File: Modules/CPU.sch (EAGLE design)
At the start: 89 parts, among them IC4 93LC66SM, IC5 MIC2026-1YM, J1 USB_A_SMT_FEMALE, J2 USB_A_SMT_FEMALE, J4 SD_CARD_SOCKET, Q1 DMG1012T-7, Q2 DMG1012T-7, Q3 DMG1012T-7, U5 LAN9512-JZX, U6 FSUSB42UMX, Y2 25MHz

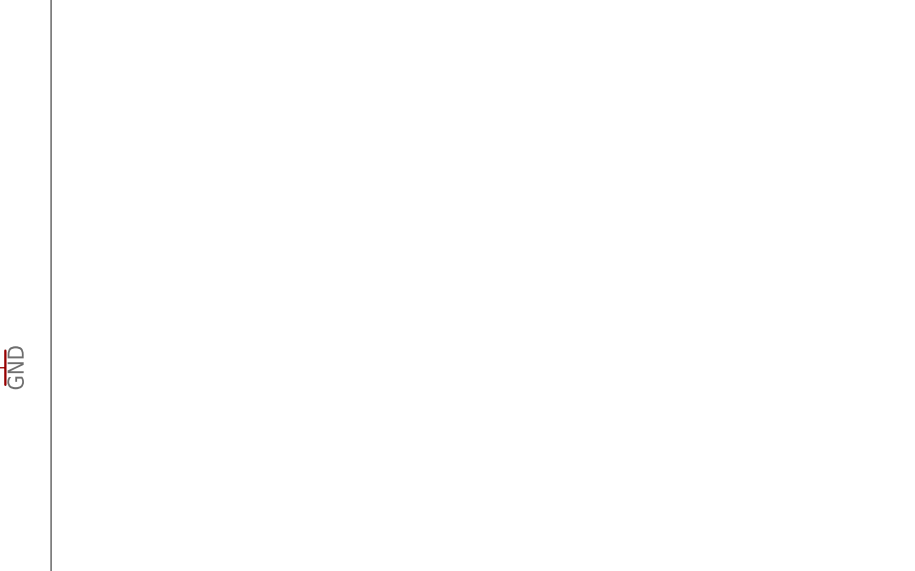
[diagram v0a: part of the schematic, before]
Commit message: Added Connectors and Molex
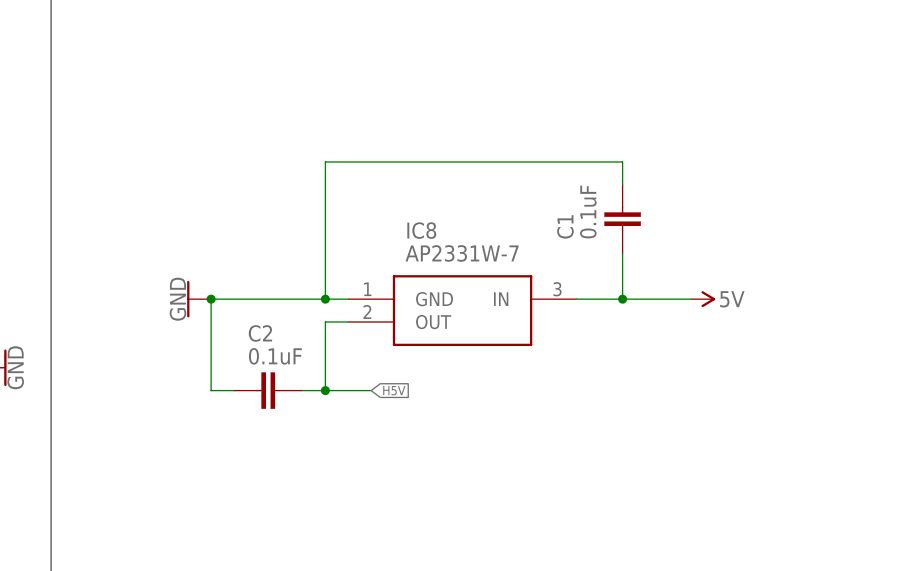
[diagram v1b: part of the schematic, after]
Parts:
- added C1, C2: 0.1uF, SparkFun-Capacitors:0.1UF-0402-16V-10%
- added IC8: AP2331W-7, SamacSys_Parts:AP2331W-7
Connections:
- new net H5V: C2.1, IC8.OUT
- net 5V: now also C1.2, IC8.IN
- net GND: now also C1.1, C2.2, IC8.GND
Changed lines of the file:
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@@
 <part name="SUPPLY4" library="SparkFun-PowerSymbols" deviceset="3.3V" device=""/>
 <part name="GND17" library="SparkFun-PowerSymbols" deviceset="GND" device=""/>
+<part name="IC8" library="SamacSys_Parts" deviceset="AP2331W-7" device=""/>
+<part name="C1" library="SparkFun-Capacitors" deviceset="0.1UF" device="-0402-16V-10%" value="0.1uF"/>
+<part name="C2" library="SparkFun-Capacitors" deviceset="0.1UF" device="-0402-16V-10%" value="0.1uF"/>
+<part name="SUPPLY5" library="SparkFun-PowerSymbols" deviceset="5V" device=""/>
+<part name="GND33" library="SparkFun-PowerSymbols" deviceset="GND" device=""/>
 </parts>
 <sheets>
@@
 <attribute name="VALUE" x="314.706" y="414.02" size="1.778" layer="96" rot="R270" align="top-center"/>
 </instance>
+<instance part="IC8" gate="G$1" x="330.2" y="246.38" smashed="yes">
+<attribute name="NAME" x="336.55" y="254" size="1.778" layer="95" align="center-left"/>
+<attribute name="VALUE" x="336.55" y="251.46" size="1.778" layer="96" align="center-left"/>
+</instance>
+<instance part="C1" gate="G$1" x="360.68" y="254" smashed="yes">
+<attribute name="NAME" x="355.219" y="252.984" size="1.778" layer="95" font="vector" rot="R90"/>
+<attribute name="VALUE" x="357.759" y="252.984" size="1.778" layer="96" font="vector" rot="R90"/>
+</instance>
+<instance part="C2" gate="G$1" x="320.04" y="236.22" smashed="yes" rot="R270">
+<attribute name="NAME" x="319.024" y="241.681" size="1.778" layer="95" font="vector"/>
+<attribute name="VALUE" x="319.024" y="239.141" size="1.778" layer="96" font="vector"/>
+</instance>
+<instance part="SUPPLY5" gate="G$1" x="368.3" y="246.38" smashed="yes" rot="R270">
+<attribute name="VALUE" x="371.348" y="246.38" size="1.778" layer="96" align="center-left"/>
+</instance>
+<instance part="GND33" gate="1" x="312.42" y="246.38" smashed="yes" rot="R270">
+<attribute name="VALUE" x="312.166" y="246.38" size="1.778" layer="96" rot="R270" align="top-center"/>
+</instance>
 </instances>
 <busses>
@@
 <wire x1="317.5" y1="414.02" x2="320.04" y2="414.02" width="0.1524" layer="91"/>
 </segment>
+<segment>
+<pinref part="IC8" gate="G$1" pin="GND"/>
+<wire x1="330.2" y1="246.38" x2="327.66" y2="246.38" width="0.1524" layer="91"/>
+<wire x1="327.66" y1="246.38" x2="327.66" y2="261.62" width="0.1524" layer="91"/>
+<wire x1="327.66" y1="261.62" x2="360.68" y2="261.62" width="0.1524" layer="91"/>
+<pinref part="C1" gate="G$1" pin="1"/>
+<wire x1="360.68" y1="261.62" x2="360.68" y2="259.08" width="0.1524" layer="91"/>
+<pinref part="GND33" gate="1" pin="GND"/>
+<wire x1="314.96" y1="246.38" x2="327.66" y2="246.38" width="0.1524" layer="91"/>
+<junction x="327.66" y="246.38"/>
+<pinref part="C2" gate="G$1" pin="2"/>
+<wire x1="317.5" y1="236.22" x2="314.96" y2="236.22" width="0.1524" layer="91"/>
+<wire x1="314.96" y1="236.22" x2="314.96" y2="246.38" width="0.1524" layer="91"/>
+<junction x="314.96" y="246.38"/>
+</segment>
 </net>
 <net name="SDA1" class="0">
@@
 <pinref part="J7" gate="G$1" pin="18"/>
 </segment>
+<segment>
+<pinref part="SUPPLY5" gate="G$1" pin="5V"/>
+<pinref part="IC8" gate="G$1" pin="IN"/>
+<wire x1="368.3" y1="246.38" x2="360.68" y2="246.38" width="0.1524" layer="91"/>
+<pinref part="C1" gate="G$1" pin="2"/>
+<wire x1="360.68" y1="246.38" x2="355.6" y2="246.38" width="0.1524" layer="91"/>
+<wire x1="360.68" y1="246.38" x2="360.68" y2="251.46" width="0.1524" layer="91"/>
+<junction x="360.68" y="246.38"/>
+</segment>
 </net>
 <net name="3.3V" class="0">
@@
 </segment>
 </net>
+<net name="H5V" class="0">
+<segment>
+<pinref part="IC8" gate="G$1" pin="OUT"/>
+<wire x1="330.2" y1="243.84" x2="327.66" y2="243.84" width="0.1524" layer="91"/>
+<wire x1="327.66" y1="243.84" x2="327.66" y2="236.22" width="0.1524" layer="91"/>
+<wire x1="327.66" y1="236.22" x2="332.74" y2="236.22" width="0.1524" layer="91"/>
+<label x="332.74" y="236.22" size="1.016" layer="95" xref="yes"/>
+<pinref part="C2" gate="G$1" pin="1"/>
+<wire x1="327.66" y1="236.22" x2="325.12" y2="236.22" width="0.1524" layer="91"/>
+<junction x="327.66" y="236.22"/>
+</segment>
+</net>

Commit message: Merged HDMI
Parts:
- added IC1: ESD5384NCTBG, SamacSys_Parts:ESD5384NCTBG
- added Q4, Q5: DMG1012T-7, SamacSys_Parts:DMG1012T-7
- added R2: 100K, SparkFun-Resistors:100KOHM-0402-1/16W-1%
- added U$6: HDMI-A, connectors:HDMI-A
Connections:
- new net HDMI_CEC: CPU1.171/HDMI_CEC, Q4.S
- new net HDMI_CK_N: CPU1.111/HDMI_CK_N*, U$6.CLOCK-
- new net HDMI_CK_P: CPU1.113/HDMI_CK_P*, U$6.CLOCK+
- new net HDMI_D0_N: CPU1.117/HDMI_D0_N*, U$6.DATA0-
- new net HDMI_D0_P: CPU1.119/HDMI_D0_P*, U$6.DATA0+
- new net HDMI_D1_N: CPU1.123/HDMI_D1_N*, U$6.DATA1-
- new net HDMI_D1_P: CPU1.125/HDMI_D1_P*, U$6.DATA1+
- new net HDMI_D2_N: CPU1.129/HDMI_D2_N*, U$6.DATA2-
- new net HDMI_D2_P: CPU1.131/HDMI_D2_P*, U$6.DATA2+
- new net HDMI_HPD_N_1V8: CPU1.88/GPIO46_1V8, Q5.D, R2.2
- new net HDMI_SCL: CPU1.175/HDMI_SCL, IC1.SDA, U$6.SDA
- new net HDMI_SDA: CPU1.173/HDMI_SDA, IC1.SCL, U$6.SCL
- new net N$6: IC1.HPD, Q5.G, U$6.HOTPLUG
- new net N$9: IC1.CEC, Q4.D, U$6.CEC
- net 1.8V: now also R2.1
- net GND: now also IC1.GND_1, IC1.GND_2, Q5.S, U$6.CECGND, U$6.CLOCKSHIELD, U$6.DATA0SHIELD, U$6.DATA1SHIELD, U$6.DATA2SHIELD
- net H5V: now also IC1.5V, IC1.RPU, Q4.G, U$6.VCC
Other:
- note added: "HDMI"
- moved on the sheet: J7

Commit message: Work
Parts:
- added SJ10: (no value), jumper:SJ
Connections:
- net HDMI_CEC: now also SJ10.2
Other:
- note added: "Board Pin Connectors"
- moved on the sheet: C1, C2, IC8, J7, J8

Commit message: Fixed CAM connectors
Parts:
- removed D11_LINK: GREEN, SparkFun-LED:LED-GREEN0603
- removed D12_FASTETHER: Yellow, SparkFun-LED:LED-YELLOW0603
- removed SJ2, SJ3, SJ4, SJ5, SJ6, SJ7, SJ8, SJ9: (no value), jumper:SJ
- added C3: 0.022uF/50V, SparkFun-Capacitors:47UF
- added J5: MAGJACK, SparkFun-Connectors:MAGJACK
- added R12, R15: 332R, adafruit:R-US_R0603
- added R18, R35, R37, R38: 0R, adafruit:R-US_R0603
- added R3, R4, R5, R6: 49.9R, adafruit:R-US_R0603
- added R36, R39: 0$, adafruit:R-US_R0603
- added R9: 10R, adafruit:R-US_R0603
- R33, R34: value 332R -> 0R
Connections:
- removed net ETH_VDD3A: C19.2, C20.2, C21.2, C22.2, C23.2, C24.2, C25.2, FB2.2, U5.VDD33A_1, U5.VDD33A_2, U5.VDD33A_3, U5.VDD33A_4, U5.VDD33A_5, U5.VDD33A_6, U5.VDD33A_7
- removed net N$25: D12_FASTETHER.C, R33.2
- removed net N$27: D11_LINK.C, R34.2
- removed net N$29: R34.1, U5.NLNKA_LED/GPIO1
- removed net N$30: R33.1, U5.NSPD_LED/GPIO2
- new net ETH_VDD33A: C19.2, C20.2, C21.2, C22.2, C23.2, C24.2, C25.2, FB2.2, R3.2, R4.2, R5.2, R6.2, R9.2, U5.VDD33A_1, U5.VDD33A_2, U5.VDD33A_3, U5.VDD33A_4, U5.VDD33A_5, U5.VDD33A_6, U5.VDD33A_7
- new net N$15: J5.GLED-, R15.1
- new net N$3: C3.2, J5.RCT, J5.TCT, R9.1
- new net NLNKA: R15.2, U5.NLNKA_LED/GPIO1
- new net NSPD: J5.YLED-, R12.1, R12.2, U5.NSPD_LED/GPIO2
- net 3.3V: now also J5.GLED+, J5.YLED+; no longer D11_LINK.A, D12_FASTETHER.A
- net CAM0_IO0: now also R35.2; no longer SJ9.1
- net CAM0_IO1: now also R36.2; no longer SJ8.1
- net CAM0_SCL: now also R37.2; no longer SJ7.1
- net CAM0_SDA: now also R38.2; no longer SJ6.1
- net CAM1_IO0: now also R39.2; no longer SJ5.1
- net CAM1_IO1: now also R34.2; no longer SJ4.1
- net CAM1_SCL: now also R33.2; no longer SJ3.1
- net CAM1_SDA: now also R18.2; no longer SJ2.1
- net GND: now also C3.1, J5.SHIELD@0, J5.SHIELD@1
- net GPIO0: now also R18.1; no longer SJ2.2
- net GPIO1: now also R33.1; no longer SJ3.2
- net GPIO28: now also R38.1; no longer SJ6.2
- net GPIO29: now also R37.1; no longer SJ7.2
- net GPIO30: now also R36.1; no longer SJ8.2
- net GPIO31: now also R35.1; no longer SJ9.2
- net GPIO4: now also R34.1; no longer SJ4.2
- net GPIO5: now also R39.1; no longer SJ5.2
- net RX_N: now also J5.RD-, R6.1
- net RX_P: now also J5.RD+, R5.1
- net TX_N: now also J5.TD-, R4.1
- net TX_P: now also J5.TD+, R3.1
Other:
- moved on the sheet: C17, C18, C19, C20, C21, C22, C23, C24, C25, C26, C27, C28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

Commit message: Got a lot of routing done
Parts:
- removed R18, R33, R34, R35, R37, R38: 0R, adafruit:R-US_R0603
- removed R36, R39: 0$, adafruit:R-US_R0603
- removed SJ10: (no value), jumper:SJ
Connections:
- net CM0_D0_P renamed CAM0_D0_P
- removed net CAM0_IO0: CAM0.17, R35.2
- removed net CAM0_IO1: CAM0.18, R36.2
- removed net CAM0_SCL: CAM0.20, R37.2
- removed net CAM0_SDA: CAM0.21, R38.2
- removed net CAM1_IO0: CAM1.17, R39.2
- removed net CAM1_IO1: CAM1.18, R34.2
- removed net CAM1_SCL: CAM1.20, R33.2
- removed net CAM1_SDA: CAM1.21, R18.2
- new net N$12: J5.YLED-, R12.1
- net GPIO0: now also CAM1.21; no longer R18.1
- net GPIO1: now also CAM1.20; no longer R33.1
- net GPIO28: now also CAM0.21; no longer R38.1
- net GPIO29: now also CAM0.20; no longer R37.1
- net GPIO30: now also CAM0.18; no longer R36.1
- net GPIO31: now also CAM0.17; no longer R35.1
- net GPIO4: now also CAM1.18; no longer R34.1
- net GPIO5: now also CAM1.17; no longer R39.1
- net HDMI_CEC: no longer SJ10.2
- net NSPD: no longer J5.YLED-, R12.1
- net RX_N: no longer J7.8
- net RX_P: no longer J7.9
- net TX_N: no longer J7.4
- net TX_P: no longer J7.5
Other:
- note added: "Note: Place 49.9 ohm resistors near LAN9512 Place 10 ohm resistor near transformers"
- moved on the sheet: C1, C2, IC8

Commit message: More routing
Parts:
- removed C12: 4.7uF, SparkFun-Capacitors:4.7UF-0603-6.3V-(10%)
- removed J4: SD_CARD_SOCKET, SparkFun-Connectors:SD_CARD_SOCKET
- added C4: 4.7uF, SparkFun-Capacitors:4.7UF-0603-6.3V-(10%)
- added J6: 503182-1853, 503182-1853:503182-1853
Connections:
- net ETH_USBDM renamed ETH_USBD_N
- net ETH_USBDP renamed ETH_USBD_P
- net ETH_USB_DM2 renamed ETH_USB_D2_N
- net ETH_USB_DM3 renamed ETH_USB_D3_N
- net ETH_USB_DP2 renamed ETH_USB_D2_P
- net ETH_USB_DP3 renamed ETH_USB_D3_P
- net 3.3V: now also C4.1, J6.VDD; no longer C12.1, J4.VDD
- net GND: now also C4.2, J6.SHIELD, J6.VSS; no longer C12.2, J4.SH@1, J4.SH@2, J4.VSS1, J4.VSS2
- net SD_CLK: now also J6.CLK; no longer J4.CLK
- net SD_CMD: now also J6.CMD; no longer J4.CMD
- net SD_D0: now also J6.DAT0; no longer J4.DAT0
- net SD_D1: now also J6.DAT1; no longer J4.DAT1
- net SD_D2: now also J6.DATA2; no longer J4.DAT2
- net SD_D3: now also J6.CD/DAT3; no longer J4.CD/DAT3
